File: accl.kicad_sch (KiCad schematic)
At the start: 0 parts

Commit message: Added Theo's ADXL sheet
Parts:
- added C? (x2): (no value), symbol Device:C_Small
- added U?: (no value), symbol Sensor_Motion:ADXL343
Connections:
- new net +3V3: C?.1, C?.1, U?.1 (Vdd_I/O), U?.12 (SDO/ADDR), U?.3 (RES), U?.6 (Vs), U?.7 (~{CS})
- new net GND: C?.2, C?.2, U?.2 (GND), U?.4 (GND), U?.5 (GND)
- new net SCL: U?.14 (SCL/SCLK)
- new net SDA: U?.13 (SDA/SDI/SDIO)
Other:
- note added: "find GPIO for interrupt pins"
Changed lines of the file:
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@@
   (title_block
     (title "Pheonix ADXL")
-  )
-  (hierarchical_label "{I2C}" (shape bidirectional) (at 27.94 29.21 180)
-    (effects (font (size 1.27 1.27)) (justify right))
+    (comment 1 "2022/10/20 TT")
+    (comment 2 "2022/10/20 WH")
+  )
+  (junction (at 52.07 29.21) (diameter 0) (color 0 0 0 0)
+  )
+  (junction (at 76.2 29.21) (diameter 0) (color 0 0 0 0)
+  )
+  (junction (at 35.56 43.18) (diameter 0) (color 0 0 0 0)
+  )
+  (junction (at 88.9 41.91) (diameter 0) (color 0 0 0 0)
+  )
+  (junction (at 46.99 29.21) (diameter 0) (color 0 0 0 0)
+  )
+  (junction (at 88.9 29.21) (diameter 0) (color 0 0 0 0)
+  )
+  (junction (at 57.15 29.21) (diameter 0) (color 0 0 0 0)
+  )
+  (bus_entry (at 24.13 43.18) (size 2.54 2.54)
+    (stroke (width 0) (type default) (color 0 0 0 0))
+  )
+  (bus_entry (at 24.13 45.72) (size 2.54 2.54)
+    (stroke (width 0) (type default) (color 0 0 0 0))
+  )
+  (wire (pts (xy 88.9 29.21) (xy 88.9 33.02))
+    (stroke (width 0) (type default) (color 0 0 0 0))
+  )
+  (wire (pts (xy 35.56 50.8) (xy 39.37 50.8))
+    (stroke (width 0) (type default) (color 0 0 0 0))
+  )
+  (wire (pts (xy 46.99 29.21) (xy 46.99 33.02))
+    (stroke (width 0) (type default) (color 0 0 0 0))
+  )
+  (wire (pts (xy 35.56 43.18) (xy 35.56 50.8))
+    (stroke (width 0) (type default) (color 0 0 0 0))
+  )
+  (wire (pts (xy 88.9 41.91) (xy 76.2 41.91))
+    (stroke (width 0) (type default) (color 0 0 0 0))
+  )
+  (wire (pts (xy 76.2 29.21) (xy 76.2 33.02))
+    (stroke (width 0) (type default) (color 0 0 0 0))
+  )
+  (wire (pts (xy 52.07 58.42) (xy 52.07 63.5))
+    (stroke (width 0) (type default) (color 0 0 0 0))
+  )
+  (wire (pts (xy 76.2 38.1) (xy 76.2 41.91))
+    (stroke (width 0) (type default) (color 0 0 0 0))
+  )
+  (wire (pts (xy 52.07 33.02) (xy 52.07 29.21))
+    (stroke (width 0) (type default) (color 0 0 0 0))
+  )
+  (wire (pts (xy 35.56 29.21) (xy 35.56 43.18))
+    (stroke (width 0) (type default) (color 0 0 0 0))
+  )
+  (wire (pts (xy 35.56 43.18) (xy 39.37 43.18))
+    (stroke (width 0) (type default) (color 0 0 0 0))
+  )
+  (wire (pts (xy 26.67 45.72) (xy 39.37 45.72))
+    (stroke (width 0) (type default) (color 0 0 0 0))
+  )
+  (wire (pts (xy 57.15 25.4) (xy 57.15 29.21))
+    (stroke (width 0) (type default) (color 0 0 0 0))
+  )
+  (wire (pts (xy 26.67 48.26) (xy 39.37 48.26))
+    (stroke (width 0) (type default) (color 0 0 0 0))
+  )
+  (wire (pts (xy 52.07 29.21) (xy 57.15 29.21))
+    (stroke (width 0) (type default) (color 0 0 0 0))
+  )
+  (wire (pts (xy 88.9 24.13) (xy 88.9 29.21))
+    (stroke (width 0) (type default) (color 0 0 0 0))
+  )
+  (wire (pts (xy 35.56 29.21) (xy 46.99 29.21))
+    (stroke (width 0) (type default) (color 0 0 0 0))
+  )
+  (wire (pts (xy 76.2 29.21) (xy 88.9 29.21))
+    (stroke (width 0) (type default) (color 0 0 0 0))
+  )
+  (wire (pts (xy 88.9 38.1) (xy 88.9 41.91))
+    (stroke (width 0) (type default) (color 0 0 0 0))
+  )
+  (wire (pts (xy 52.07 29.21) (xy 46.99 29.21))
+    (stroke (width 0) (type default) (color 0 0 0 0))
+  )
+  (bus (pts (xy 24.13 43.18) (xy 24.13 45.72))
+    (stroke (width 0) (type default) (color 0 0 0 0))
+  )
+  (wire (pts (xy 88.9 41.91) (xy 88.9 46.99))
+    (stroke (width 0) (type default) (color 0 0 0 0))
+  )
+  (wire (pts (xy 57.15 29.21) (xy 57.15 33.02))
+    (stroke (width 0) (type default) (color 0 0 0 0))
+  )
+  (wire (pts (xy 57.15 29.21) (xy 76.2 29.21))
+    (stroke (width 0) (type default) (color 0 0 0 0))
+  )
+  (bus (pts (xy 24.13 40.64) (xy 24.13 43.18))
+    (stroke (width 0) (type default) (color 0 0 0 0))
+  )
+  (text "find GPIO for interrupt pins" (at 64.77 55.88 0)
+    (effects (font (size 1.27 1.27)) (justify left bottom))
+  )
+  (label "SCL" (at 29.21 48.26 0)
+    (effects (font (size 1.27 1.27)) (justify left bottom))
+  )
+  (label "SDA" (at 29.21 45.72 0)
+    (effects (font (size 1.27 1.27)) (justify left bottom))
+  )
+  (hierarchical_label "{I2C}" (shape bidirectional) (at 24.13 40.64 90)
+    (effects (font (size 1.27 1.27)) (justify left))
+  )
+  (symbol (lib_id "power:+3V3") (at 57.15 25.4 0) (unit 1)
+    (in_bom yes) (on_board yes) (fields_autoplaced)
+    (property "Reference" "#PWR?" (id 0) (at 57.15 29.21 0)
+      (effects (font (size 1.27 1.27)) hide)
+    )
+    (property "Value" "" (id 1) (at 57.15 20.32 0))
+    (property "Footprint" "" (id 2) (at 57.15 25.4 0)
+      (effects (font (size 1.27 1.27)) hide)
+    )
+    (property "Datasheet" "" (id 3) (at 57.15 25.4 0)
+      (effects (font (size 1.27 1.27)) hide)
+    )
+    (pin "1")
+  )
+  (symbol (lib_id "Sensor_Motion:ADXL343") (at 52.07 45.72 0) (unit 1)
+    (in_bom yes) (on_board yes) (fields_autoplaced)
+    (property "Reference" "U?" (id 0) (at 67.31 39.1412 0))
+    (property "Value" "" (id 1) (at 67.31 41.6812 0))
+    (property "Footprint" "" (id 2) (at 52.07 45.72 0)
+      (effects (font (size 1.27 1.27)) hide)
+    )
+    (property "Datasheet" "https://www.analog.com/media/en/technical-documentation/data-sheets/ADXL343.pdf" (id 3) (at 52.07 45.72 0)
+      (effects (font (size 1.27 1.27)) hide)
+    )
+    (pin "1")
+    (pin "10")
+    (pin "11")
+    (pin "12")
+    (pin "13")
+    (pin "14")
+    (pin "2")
+    (pin "3")
+    (pin "4")
+    (pin "5")
+    (pin "6")
+    (pin "7")
+    (pin "8")
+    (pin "9")
+  )
+  (symbol (lib_id "Device:C_Small") (at 88.9 35.56 0) (unit 1)
+    (in_bom yes) (on_board yes) (fields_autoplaced)
+    (property "Reference" "C?" (id 0) (at 91.44 34.2962 0)
+      (effects (font (size 1.27 1.27)) (justify left))
+    )
+    (property "Value" "" (id 1) (at 91.44 36.8362 0)
+      (effects (font (size 1.27 1.27)) (justify left))
+    )
+    (property "Footprint" "" (id 2) (at 88.9 35.56 0)
+      (effects (font (size 1.27 1.27)) hide)
+    )
+    (property "Datasheet" "~" (id 3) (at 88.9 35.56 0)
+      (effects (font (size 1.27 1.27)) hide)
+    )
+    (pin "1")
+    (pin "2")
+  )
+  (symbol (lib_id "power:GND") (at 52.07 63.5 0) (unit 1)
+    (in_bom yes) (on_board yes) (fields_autoplaced)
+    (property "Reference" "#PWR?" (id 0) (at 52.07 69.85 0)
+      (effects (font (size 1.27 1.27)) hide)
+    )
+    (property "Value" "" (id 1) (at 52.07 68.58 0))
+    (property "Footprint" "" (id 2) (at 52.07 63.5 0)
+      (effects (font (size 1.27 1.27)) hide)
+    )
+    (property "Datasheet" "" (id 3) (at 52.07 63.5 0)
+      (effects (font (size 1.27 1.27)) hide)
+    )
+    (pin "1")
+  )
+  (symbol (lib_id "power:+3V3") (at 88.9 24.13 0) (unit 1)
+    (in_bom yes) (on_board yes) (fields_autoplaced)
+    (property "Reference" "#PWR?" (id 0) (at 88.9 27.94 0)
+      (effects (font (size 1.27 1.27)) hide)
+    )
+    (property "Value" "" (id 1) (at 88.9 19.05 0))
+    (property "Footprint" "" (id 2) (at 88.9 24.13 0)
+      (effects (font (size 1.27 1.27)) hide)
+    )
+    (property "Datasheet" "" (id 3) (at 88.9 24.13 0)
+      (effects (font (size 1.27 1.27)) hide)
+    )
+    (pin "1")
+  )
+  (symbol (lib_id "power:GND") (at 88.9 46.99 0) (unit 1)
+    (in_bom yes) (on_board yes) (fields_autoplaced)
+    (property "Reference" "#PWR?" (id 0) (at 88.9 53.34 0)
+      (effects (font (size 1.27 1.27)) hide)
+    )
+    (property "Value" "" (id 1) (at 88.9 52.07 0))
+    (property "Footprint" "" (id 2) (at 88.9 46.99 0)
+      (effects (font (size 1.27 1.27)) hide)
+    )
+    (property "Datasheet" "" (id 3) (at 88.9 46.99 0)
+      (effects (font (size 1.27 1.27)) hide)
+    )
+    (pin "1")
+  )
+  (symbol (lib_id "Device:C_Small") (at 76.2 35.56 0) (unit 1)
+    (in_bom yes) (on_board yes) (fields_autoplaced)
+    (property "Reference" "C?" (id 0) (at 78.74 34.2962 0)
+      (effects (font (size 1.27 1.27)) (justify left))
+    )
+    (property "Value" "" (id 1) (at 78.74 36.8362 0)
+      (effects (font (size 1.27 1.27)) (justify left))
+    )
+    (property "Footprint" "" (id 2) (at 76.2 35.56 0)
+      (effects (font (size 1.27 1.27)) hide)
+    )
+    (property "Datasheet" "~" (id 3) (at 76.2 35.56 0)
+      (effects (font (size 1.27 1.27)) hide)
+    )
+    (pin "1")
+    (pin "2")
   )
 )

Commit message: Various updates because I forgot to commit for a while
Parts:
- C17, C18: renamed from C?; value (none) -> 100nF
- U6: renamed from U?; value (none) -> ADXL343; footprint (none) -> Package_LGA:LGA-14_3x5mm_P0.8mm_LayoutBorder1x6y
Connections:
- net GND: now also U6.11 (RES)
- net Accel1: now reaches U6.8 (INT1)
- net Accel2: now reaches U6.9 (INT2)
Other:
- note removed: "find GPIO for interrupt pins"
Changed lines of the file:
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@@
     (comment 2 "2022/10/20 WH")
   )
+  (junction (at 52.07 60.96) (diameter 0) (color 0 0 0 0)
+  )
   (junction (at 52.07 29.21) (diameter 0) (color 0 0 0 0)
   )
@@
     (stroke (width 0) (type default) (color 0 0 0 0))
   )
+  (bus_entry (at 73.66 50.8) (size -2.54 -2.54)
+    (stroke (width 0) (type default) (color 0 0 0 0))
+  )
+  (bus_entry (at 73.66 48.26) (size -2.54 -2.54)
+    (stroke (width 0) (type default) (color 0 0 0 0))
+  )
   (wire (pts (xy 88.9 29.21) (xy 88.9 33.02))
     (stroke (width 0) (type default) (color 0 0 0 0))
   )
+  (wire (pts (xy 64.77 45.72) (xy 71.12 45.72))
+    (stroke (width 0) (type default) (color 0 0 0 0))
+  )
+  (bus (pts (xy 73.66 50.8) (xy 73.66 53.34))
+    (stroke (width 0) (type default) (color 0 0 0 0))
+  )
   (wire (pts (xy 35.56 50.8) (xy 39.37 50.8))
     (stroke (width 0) (type default) (color 0 0 0 0))
@@
     (stroke (width 0) (type default) (color 0 0 0 0))
   )
-  (wire (pts (xy 52.07 58.42) (xy 52.07 63.5))
+  (wire (pts (xy 52.07 58.42) (xy 52.07 60.96))
     (stroke (width 0) (type default) (color 0 0 0 0))
   )
@@
     (stroke (width 0) (type default) (color 0 0 0 0))
   )
+  (wire (pts (xy 52.07 60.96) (xy 57.15 60.96))
+    (stroke (width 0) (type default) (color 0 0 0 0))
+  )
   (wire (pts (xy 26.67 45.72) (xy 39.37 45.72))
     (stroke (width 0) (type default) (color 0 0 0 0))
   )
+  (bus (pts (xy 73.66 48.26) (xy 73.66 50.8))
+    (stroke (width 0) (type default) (color 0 0 0 0))
+  )
+  (wire (pts (xy 57.15 60.96) (xy 57.15 58.42))
+    (stroke (width 0) (type default) (color 0 0 0 0))
+  )
+  (wire (pts (xy 52.07 60.96) (xy 52.07 63.5))
+    (stroke (width 0) (type default) (color 0 0 0 0))
+  )
   (wire (pts (xy 57.15 25.4) (xy 57.15 29.21))
     (stroke (width 0) (type default) (color 0 0 0 0))
@@
     (stroke (width 0) (type default) (color 0 0 0 0))
   )
+  (wire (pts (xy 64.77 48.26) (xy 71.12 48.26))
+    (stroke (width 0) (type default) (color 0 0 0 0))
+  )
   (wire (pts (xy 88.9 41.91) (xy 88.9 46.99))
     (stroke (width 0) (type default) (color 0 0 0 0))
@@
     (stroke (width 0) (type default) (color 0 0 0 0))
   )
-  (text "find GPIO for interrupt pins" (at 64.77 55.88 0)
-    (effects (font (size 1.27 1.27)) (justify left bottom))
-  )
   (label "SCL" (at 29.21 48.26 0)
     (effects (font (size 1.27 1.27)) (justify left bottom))
   )
   (label "SDA" (at 29.21 45.72 0)
+    (effects (font (size 1.27 1.27)) (justify left bottom))
+  )
+  (label "Accel1" (at 64.77 45.72 0)
+    (effects (font (size 1.27 1.27)) (justify left bottom))
+  )
+  (label "Accel2" (at 64.77 48.26 0)
     (effects (font (size 1.27 1.27)) (justify left bottom))
   )
@@
     (effects (font (size 1.27 1.27)) (justify left))
   )
+  (hierarchical_label "{INT}" (shape output) (at 73.66 53.34 270)
+    (effects (font (size 1.27 1.27)) (justify right))
+  )
   (symbol (lib_id "power:+3V3") (at 57.15 25.4 0) (unit 1)
     (in_bom yes) (on_board yes) (fields_autoplaced)
-    (property "Reference" "#PWR?" (id 0) (at 57.15 29.21 0)
-      (effects (font (size 1.27 1.27)) hide)
-    )
-    (property "Value" "" (id 1) (at 57.15 20.32 0))
+    (property "Reference" "#PWR035" (id 0) (at 57.15 29.21 0)
+      (effects (font (size 1.27 1.27)) hide)
+    )
+    (property "Value" "+3V3" (id 1) (at 57.15 20.32 0))
     (property "Footprint" "" (id 2) (at 57.15 25.4 0)
       (effects (font (size 1.27 1.27)) hide)
@@
   (symbol (lib_id "Sensor_Motion:ADXL343") (at 52.07 45.72 0) (unit 1)
     (in_bom yes) (on_board yes) (fields_autoplaced)
-    (property "Reference" "U?" (id 0) (at 67.31 39.1412 0))
-    (property "Value" "" (id 1) (at 67.31 41.6812 0))
-    (property "Footprint" "" (id 2) (at 52.07 45.72 0)
+    (property "Reference" "U6" (id 0) (at 67.31 39.1412 0))
+    (property "Value" "ADXL343" (id 1) (at 67.31 41.6812 0))
+    (property "Footprint" "Package_LGA:LGA-14_3x5mm_P0.8mm_LayoutBorder1x6y" (id 2) (at 52.07 45.72 0)
       (effects (font (size 1.27 1.27)) hide)
     )
@@
   (symbol (lib_id "Device:C_Small") (at 88.9 35.56 0) (unit 1)
     (in_bom yes) (on_board yes) (fields_autoplaced)
-    (property "Reference" "C?" (id 0) (at 91.44 34.2962 0)
-      (effects (font (size 1.27 1.27)) (justify left))
-    )
-    (property "Value" "" (id 1) (at 91.44 36.8362 0)
+    (property "Reference" "C18" (id 0) (at 91.44 34.2962 0)
+      (effects (font (size 1.27 1.27)) (justify left))
+    )
+    (property "Value" "100nF" (id 1) (at 91.44 36.8362 0)
       (effects (font (size 1.27 1.27)) (justify left))
     )
@@
   (symbol (lib_id "power:GND") (at 52.07 63.5 0) (unit 1)
     (in_bom yes) (on_board yes) (fields_autoplaced)
-    (property "Reference" "#PWR?" (id 0) (at 52.07 69.85 0)
-      (effects (font (size 1.27 1.27)) hide)
-    )
-    (property "Value" "" (id 1) (at 52.07 68.58 0))
+    (property "Reference" "#PWR034" (id 0) (at 52.07 69.85 0)
+      (effects (font (size 1.27 1.27)) hide)
+    )
+    (property "Value" "GND" (id 1) (at 52.07 68.58 0))
     (property "Footprint" "" (id 2) (at 52.07 63.5 0)
       (effects (font (size 1.27 1.27)) hide)
@@
   (symbol (lib_id "power:+3V3") (at 88.9 24.13 0) (unit 1)
     (in_bom yes) (on_board yes) (fields_autoplaced)
-    (property "Reference" "#PWR?" (id 0) (at 88.9 27.94 0)
-      (effects (font (size 1.27 1.27)) hide)
-    )
-    (property "Value" "" (id 1) (at 88.9 19.05 0))
+    (property "Reference" "#PWR036" (id 0) (at 88.9 27.94 0)
+      (effects (font (size 1.27 1.27)) hide)
+    )
+    (property "Value" "+3V3" (id 1) (at 88.9 19.05 0))
     (property "Footprint" "" (id 2) (at 88.9 24.13 0)
       (effects (font (size 1.27 1.27)) hide)
@@
   (symbol (lib_id "power:GND") (at 88.9 46.99 0) (unit 1)
     (in_bom yes) (on_board yes) (fields_autoplaced)
-    (property "Reference" "#PWR?" (id 0) (at 88.9 53.34 0)
-      (effects (font (size 1.27 1.27)) hide)
-    )
-    (property "Value" "" (id 1) (at 88.9 52.07 0))
+    (property "Reference" "#PWR037" (id 0) (at 88.9 53.34 0)
+      (effects (font (size 1.27 1.27)) hide)
+    )
+    (property "Value" "GND" (id 1) (at 88.9 52.07 0))
     (property "Footprint" "" (id 2) (at 88.9 46.99 0)
       (effects (font (size 1.27 1.27)) hide)
@@
   (symbol (lib_id "Device:C_Small") (at 76.2 35.56 0) (unit 1)
     (in_bom yes) (on_board yes) (fields_autoplaced)
-    (property "Reference" "C?" (id 0) (at 78.74 34.2962 0)
-      (effects (font (size 1.27 1.27)) (justify left))
-    )
-    (property "Value" "" (id 1) (at 78.74 36.8362 0)
-      (effects (font (size 1.27 1.27)) (justify left))
-    )
+    (property "Reference" "C17" (id 0) (at 78.74 34.2962 0)
+      (effects (font (size 1.27 1.27)) (justify left))
+    )
+    (property "Value" "100nF" (id 1) (at 78.74 36.8362 0)
+      (effects (font (size 1.27 1.27)) (justify left))
+    )

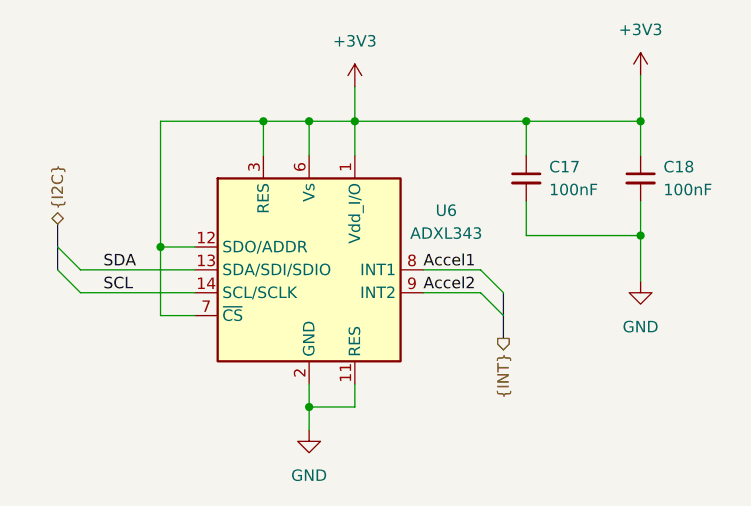
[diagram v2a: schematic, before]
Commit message: Connected the sensors, flash chip, Need to connect the radio and GPS
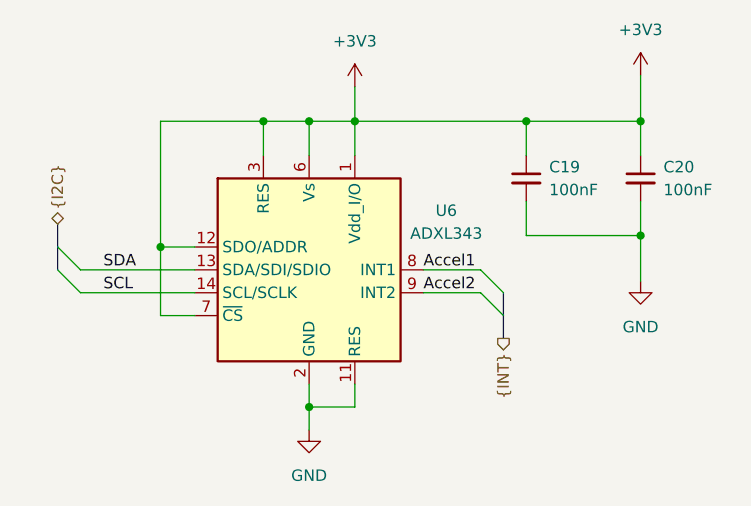
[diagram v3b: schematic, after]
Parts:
- C20: renamed from C18; footprint (none) -> Capacitor_SMD:C_0603_1608Metric
- renumbered C17 to C19
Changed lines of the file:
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@@
   (symbol (lib_id "power:+3V3") (at 57.15 25.4 0) (unit 1)
     (in_bom yes) (on_board yes) (fields_autoplaced)
-    (property "Reference" "#PWR035" (id 0) (at 57.15 29.21 0)
+    (property "Reference" "#PWR037" (id 0) (at 57.15 29.21 0)
       (effects (font (size 1.27 1.27)) hide)
     )
@@
   (symbol (lib_id "Device:C_Small") (at 88.9 35.56 0) (unit 1)
     (in_bom yes) (on_board yes) (fields_autoplaced)
-    (property "Reference" "C18" (id 0) (at 91.44 34.2962 0)
+    (property "Reference" "C20" (id 0) (at 91.44 34.2962 0)
       (effects (font (size 1.27 1.27)) (justify left))
     )
@@
       (effects (font (size 1.27 1.27)) (justify left))
     )
-    (property "Footprint" "" (id 2) (at 88.9 35.56 0)
+    (property "Footprint" "Capacitor_SMD:C_0603_1608Metric" (id 2) (at 88.9 35.56 0)
       (effects (font (size 1.27 1.27)) hide)
     )
@@
   (symbol (lib_id "power:GND") (at 52.07 63.5 0) (unit 1)
     (in_bom yes) (on_board yes) (fields_autoplaced)
-    (property "Reference" "#PWR034" (id 0) (at 52.07 69.85 0)
+    (property "Reference" "#PWR036" (id 0) (at 52.07 69.85 0)
       (effects (font (size 1.27 1.27)) hide)
     )
@@
   (symbol (lib_id "power:+3V3") (at 88.9 24.13 0) (unit 1)
     (in_bom yes) (on_board yes) (fields_autoplaced)
-    (property "Reference" "#PWR036" (id 0) (at 88.9 27.94 0)
+    (property "Reference" "#PWR038" (id 0) (at 88.9 27.94 0)
       (effects (font (size 1.27 1.27)) hide)
     )
@@
   (symbol (lib_id "power:GND") (at 88.9 46.99 0) (unit 1)
     (in_bom yes) (on_board yes) (fields_autoplaced)
-    (property "Reference" "#PWR037" (id 0) (at 88.9 53.34 0)
+    (property "Reference" "#PWR039" (id 0) (at 88.9 53.34 0)
       (effects (font (size 1.27 1.27)) hide)
     )
@@
   (symbol (lib_id "Device:C_Small") (at 76.2 35.56 0) (unit 1)
     (in_bom yes) (on_board yes) (fields_autoplaced)
-    (property "Reference" "C17" (id 0) (at 78.74 34.2962 0)
+    (property "Reference" "C19" (id 0) (at 78.74 34.2962 0)
       (effects (font (size 1.27 1.27)) (justify left))
     )

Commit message: Rearrange parts of PCB
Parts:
- C19: footprint (none) -> Capacitor_SMD:C_0603_1608Metric
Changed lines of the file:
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@@
       (effects (font (size 1.27 1.27)) (justify left))
     )
-    (property "Footprint" "" (id 2) (at 76.2 35.56 0)
+    (property "Footprint" "Capacitor_SMD:C_0603_1608Metric" (id 2) (at 76.2 35.56 0)
       (effects (font (size 1.27 1.27)) hide)
     )
